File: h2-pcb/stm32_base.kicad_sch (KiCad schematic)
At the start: 42 parts, among them J1 Network Connector, J2 STDC14, SW1 SW_Push, U1 LD39050PU33R, U2 STM32G474RBT6, U3 SN65HVD230, Y1 8MHz

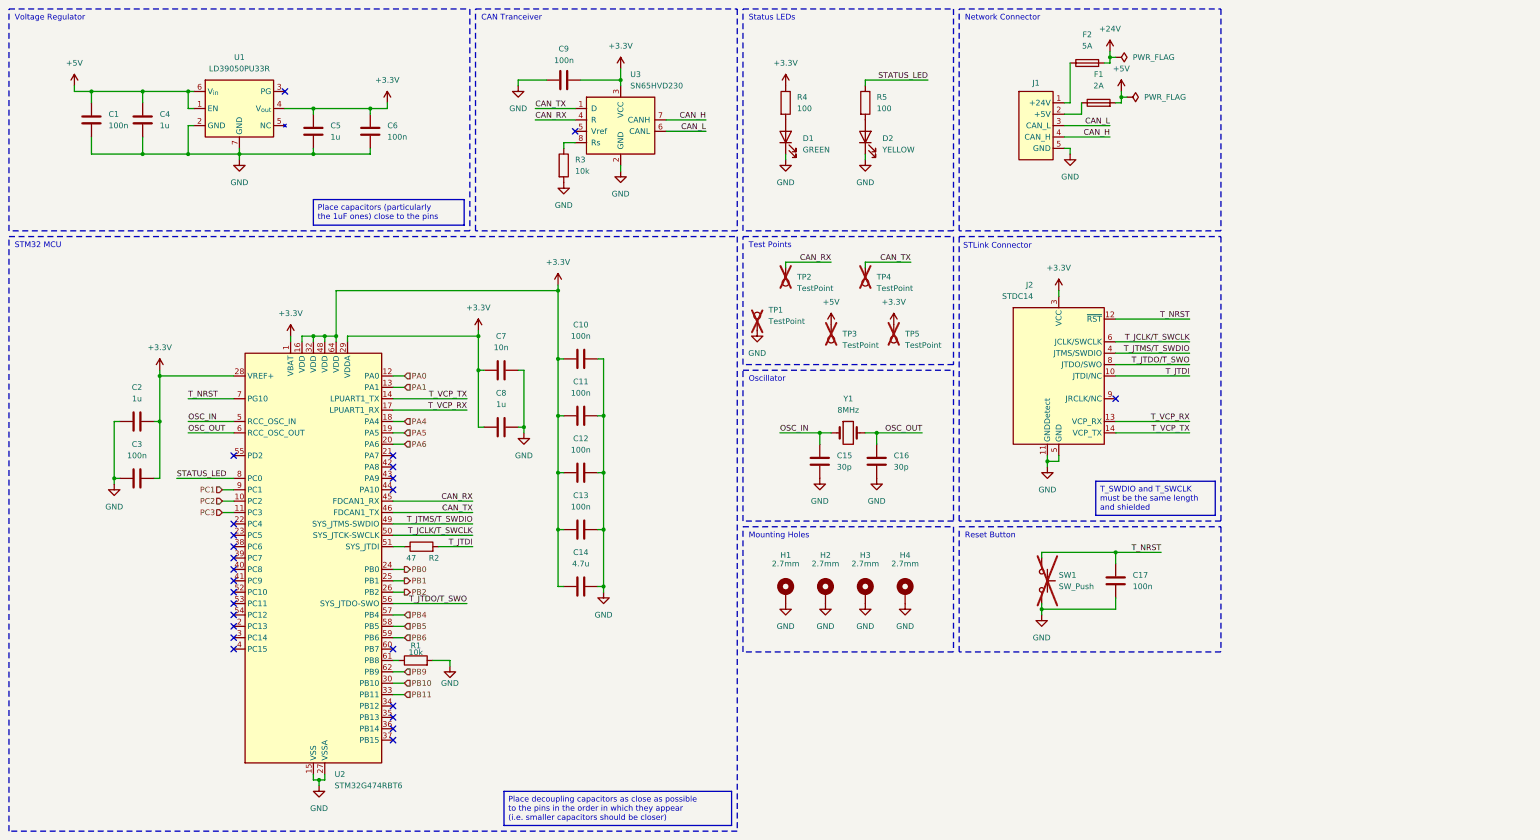
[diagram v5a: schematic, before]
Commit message: h2-pcb: add manometer, actuator and ds2428
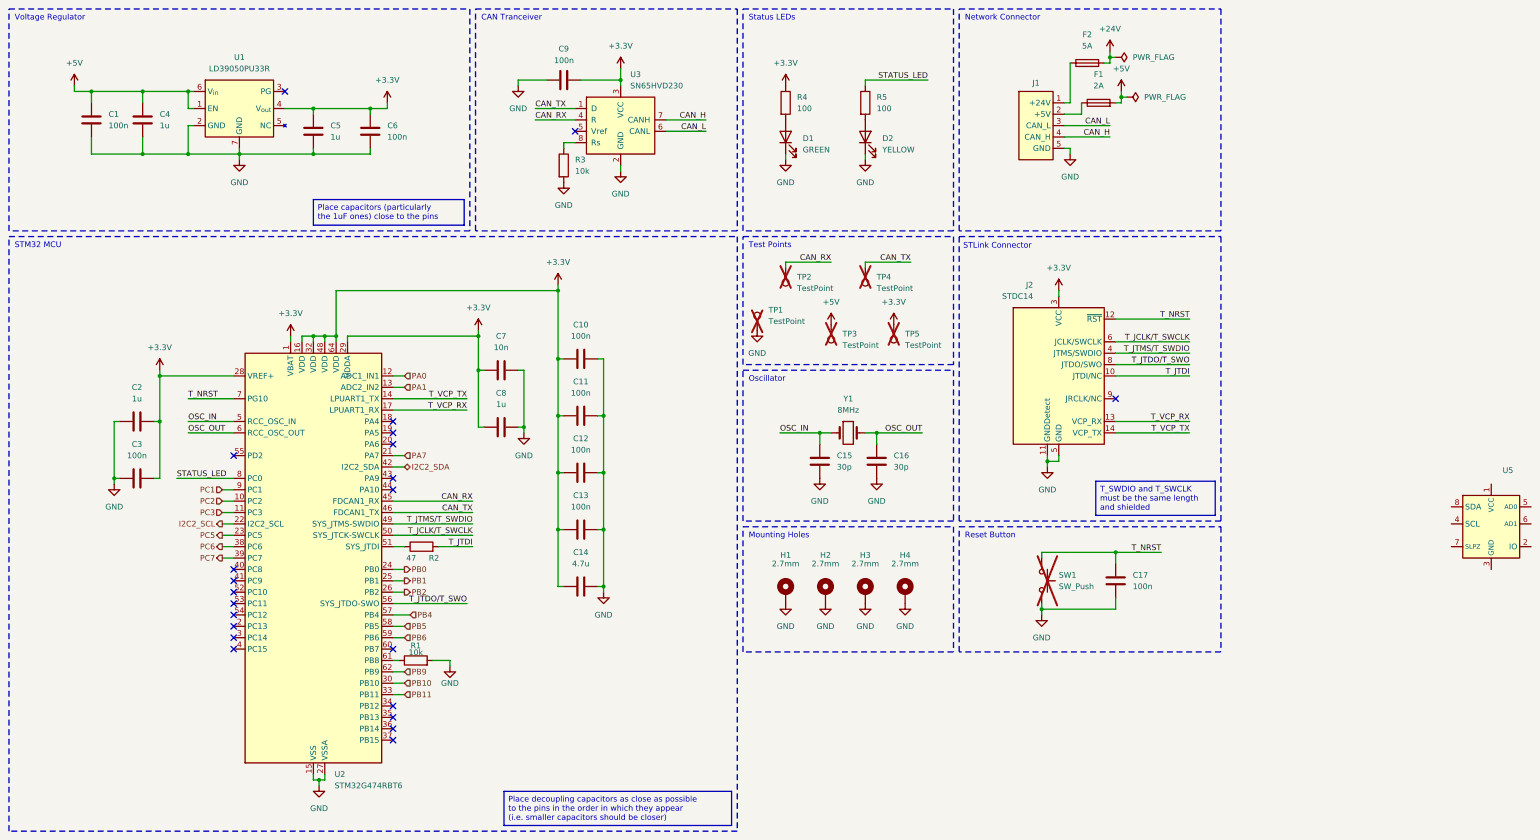
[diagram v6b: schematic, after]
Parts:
- added U5: ~, symbol DS2482-100:DS2482-100
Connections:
- net PA7: now reaches U2.21 (PA7)
- net I2C2_SCL: now reaches U2.22 (PC4)
- net PC5: now reaches U2.23 (PC5)
- net PC6: now reaches U2.38 (PC6)
- net PC7: now reaches U2.39 (PC7)
- net I2C2_SDA: now reaches U2.42 (PA8)
- net PA4: no longer names the net of U2.18 (PA4)
- net PA5: no longer names the net of U2.19 (PA5)
- net PA6: no longer names the net of U2.20 (PA6)
- no-connect marks 25 -> 22
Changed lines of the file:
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@@
 	)
 	(no_connect
-		(at 99.06 115.57)
-	)
-	(no_connect
 		(at 63.5 146.05)
 	)
 	(no_connect
-		(at 63.5 130.81)
-	)
-	(no_connect
 		(at 99.06 171.45)
 	)
@@
 	)
 	(no_connect
-		(at 63.5 128.27)
-	)
-	(no_connect
 		(at 99.06 120.65)
 	)
@@
 	)
 	(no_connect
+		(at 99.06 105.41)
+	)
+	(no_connect
 		(at 74.93 31.75)
 	)
@@
 	)
 	(no_connect
-		(at 63.5 133.35)
-	)
-	(no_connect
 		(at 99.06 176.53)
 	)
@@
 	)
 	(no_connect
-		(at 63.5 135.89)
-	)
-	(no_connect
-		(at 99.06 113.03)
+		(at 99.06 110.49)
 	)
 	(no_connect
@@
 	)
 	(no_connect
+		(at 99.06 107.95)
+	)
+	(no_connect
 		(at 63.5 151.13)
 	)
@@
 	(wire
 		(pts
-			(xy 99.06 105.41) (xy 101.6 105.41)
-		)
-		(stroke
-			(width 0)
-			(type default)
-		)
-	)
-	(wire
-		(pts
 			(xy 81.28 44.45) (xy 81.28 45.72)
 		)
@@
 	(wire
 		(pts
+			(xy 60.96 130.81) (xy 63.5 130.81)
+		)
+		(stroke
+			(width 0)
+			(type default)
+		)
+	)
+	(wire
+		(pts
 			(xy 144.78 142.24) (xy 146.05 142.24)
 		)
@@
 	(wire
 		(pts
+			(xy 60.96 128.27) (xy 63.5 128.27)
+		)
+		(stroke
+			(width 0)
+			(type default)
+		)
+	)
+	(wire
+		(pts
 			(xy 99.06 133.35) (xy 101.6 133.35)
 		)
@@
 	(wire
 		(pts
+			(xy 99.06 113.03) (xy 101.6 113.03)
+		)
+		(stroke
+			(width 0)
+			(type default)
+		)
+	)
+	(wire
+		(pts
 			(xy 82.55 185.42) (xy 81.28 185.42)
 		)
@@
 	(wire
 		(pts
-			(xy 99.06 148.59) (xy 101.6 148.59)
+			(xy 99.06 148.59) (xy 102.87 148.59)
 		)
 		(stroke
@@
 	(wire
 		(pts
+			(xy 60.96 135.89) (xy 63.5 135.89)
+		)
+		(stroke
+			(width 0)
+			(type default)
+		)
+	)
+	(wire
+		(pts
 			(xy 146.05 116.84) (xy 146.05 129.54)
 		)
@@
 	(wire
 		(pts
-			(xy 99.06 107.95) (xy 101.6 107.95)
-		)
-		(stroke
-			(width 0)
-			(type default)
-		)
-	)
-	(wire
-		(pts
 			(xy 118.11 86.36) (xy 118.11 93.98)
 		)
@@
 	(wire
 		(pts
+			(xy 60.96 133.35) (xy 63.5 133.35)
+		)
+		(stroke
+			(width 0)
+			(type default)
+		)
+	)
+	(wire
+		(pts
 			(xy 127 93.98) (xy 128.27 93.98)
 		)
@@
 	(wire
 		(pts
-			(xy 99.06 110.49) (xy 101.6 110.49)
+			(xy 135.89 142.24) (xy 137.16 142.24)
 		)
 		(stroke
@@
 	(wire
 		(pts
-			(xy 135.89 142.24) (xy 137.16 142.24)
+			(xy 99.06 123.19) (xy 116.84 123.19)
 		)
 		(stroke
@@
 	(wire
 		(pts
-			(xy 99.06 123.19) (xy 116.84 123.19)
+			(xy 186.69 71.12) (xy 186.69 69.85)
 		)
 		(stroke
@@
 	(wire
 		(pts
-			(xy 186.69 71.12) (xy 186.69 69.85)
+			(xy 99.06 115.57) (xy 101.6 115.57)
 		)
 		(stroke
@@
 		)
 	)
+	(hierarchical_label "I2C2_SDA"
+		(shape bidirectional)
+		(at 101.6 115.57 0)
+		(effects
+			(font
+				(size 1.27 1.27)
+			)
+			(justify left)
+		)
+	)
 	(hierarchical_label "PB2"
 		(shape output)
@@
 		)
 	)
-	(hierarchical_label "PA6"
+	(hierarchical_label "PC2"
 		(shape input)
-		(at 101.6 110.49 0)
+		(at 60.96 123.19 180)
 		(effects
 			(font
 				(size 1.27 1.27)
 			)
-			(justify left)
+			(justify right)
 		)
 	)
-	(hierarchical_label "PC2"
+	(hierarchical_label "PA7"
 		(shape input)
-		(at 60.96 123.19 180)
+		(at 101.6 113.03 0)
 		(effects
 			(font
 				(size 1.27 1.27)
 			)
-			(justify right)
+			(justify left)
 		)
 	)
-	(hierarchical_label "PB9"
-		(shape input)
-		(at 101.6 161.29 0)
+	(hierarchical_label "PC7"
+		(shape output)
+		(at 60.96 135.89 180)
 		(effects
 			(font
 				(size 1.27 1.27)
 			)
-			(justify left)
+			(justify right)
 		)
 	)
-	(hierarchical_label "PB10"
+	(hierarchical_label "PB9"
 		(shape input)
-		(at 101.6 163.83 0)
+		(at 101.6 161.29 0)
 		(effects
 			(font
@@
 		)
 	)
-	(hierarchical_label "PA4"
+	(hierarchical_label "PB10"
 		(shape input)
-		(at 101.6 105.41 0)
+		(at 101.6 163.83 0)
 		(effects
 			(font
@@
 	(hierarchical_label "PB4"
 		(shape input)
-		(at 101.6 148.59 0)
+		(at 102.87 148.59 0)
 		(effects
 			(font
@@
 		)
 	)
-	(hierarchical_label "PA5"
-		(shape input)
-		(at 101.6 107.95 0)
+	(hierarchical_label "PC6"
+		(shape output)
+		(at 60.96 133.35 180)
 		(effects
 			(font
 				(size 1.27 1.27)
 			)
-			(justify left)
+			(justify right)
+		)
+	)
+	(hierarchical_label "I2C2_SCL"
+		(shape output)
+		(at 60.96 128.27 180)
+		(effects
+			(font
+				(size 1.27 1.27)
+			)
+			(justify right)
+		)
+	)
+	(hierarchical_label "PC5"
+		(shape output)
+		(at 60.96 130.81 180)
+		(effects
+			(font
+				(size 1.27 1.27)
+			)
+			(justify right)
 		)
 	)
@@
 	)
 	(symbol
+		(lib_name "DS2482-100_1")
+		(lib_id "DS2482-100:DS2482-100")
+		(at 344.17 128.27 0)
+		(unit 1)
+		(exclude_from_sim no)
+		(in_bom yes)
+		(on_board yes)
+		(dnp no)
+		(property "Reference" "U5"
+			(at 346.71 116.332 0)
+			(effects
+				(font
+					(size 1.27 1.27)
+				)
+				(justify left)
+			)
+		)
+		(property "Value" "~"
+			(at 347.726 117.602 0)
+			(effects
+				(font
+					(size 1.27 1.27)
+				)
+				(justify left)
+			)
+		)
+		(property "Footprint" ""
+			(at 344.17 130.81 0)
+			(effects
+				(font
+					(size 1.27 1.27)
+				)
+				(hide yes)
+			)
+		)
+		(property "Datasheet" ""
+			(at 344.17 130.81 0)
+			(effects
+				(font
+					(size 1.27 1.27)
+				)
+				(hide yes)
+			)
+		)
+		(property "Description" ""
+			(at 344.17 130.81 0)
+			(effects
+				(font
+					(size 1.27 1.27)
+				)
+				(hide yes)
+			)
+		)
+		(pin "1"
+		)
+		(pin "2"
+		)
+		(pin "3"
+		)
+		(pin "4"
+		)
+		(pin "5"
+		)
+		(pin "6"
+		)
+		(pin "7"
+		)
+		(pin "8"
+		)
+		(instances
+			(project ""
+				(path "/4b4cf3aa-c94c-4150-b9c5-35049cd71136/7d59fd70-1fff-4c9c-ae77-583b08aef567"
+					(reference "U5")
+					(unit 1)
+				)
+			)
+		)
+	)
+	(symbol
 		(lib_id "power:PWR_FLAG")
 		(at 260.35 24.13 270)
@@
 		)
 		(pin "22"
+			(alternate "I2C2_SCL")
 		)
 		(pin "19"
@@
 		)
 		(pin "13"
+			(alternate "ADC2_IN2")
 		)
 		(pin "37"
@@
 		)
 		(pin "12"
+			(alternate "ADC1_IN1")
 		)
 		(pin "41"
 		)
 		(pin "42"
+			(alternate "I2C2_SDA")
 		)
 		(pin "5"

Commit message: Mosfets and Actuators dans truc pcb
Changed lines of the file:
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@@
 		)
 		(pin "35"
+			(alternate "ADC3_IN5")
 		)
 		(pin "1"

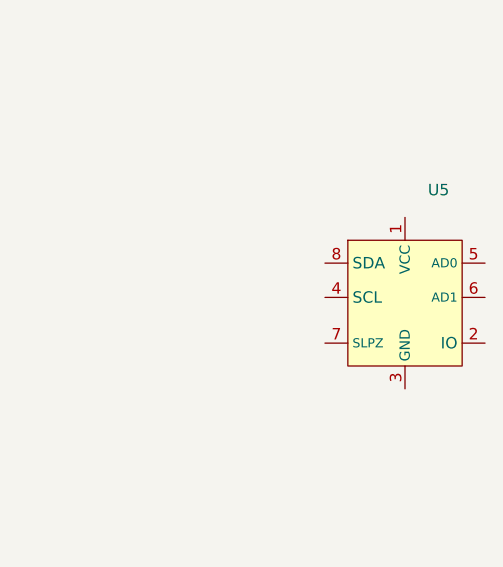
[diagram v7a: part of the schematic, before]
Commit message: Ajout des footprints aux composantes & update du pcb (routage almost done ?)
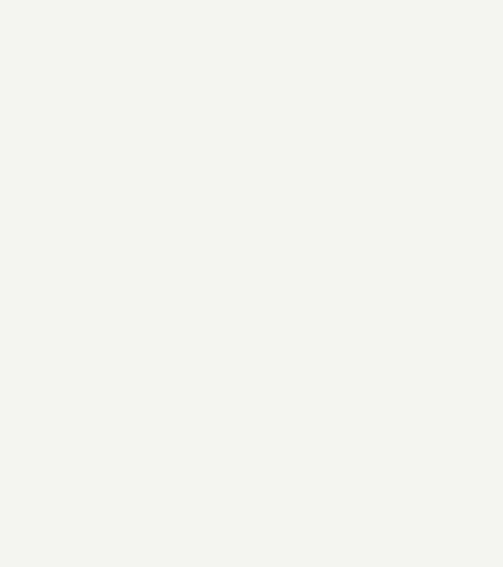
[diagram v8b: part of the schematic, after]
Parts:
- removed U5: ~, symbol DS2482-100:DS2482-100
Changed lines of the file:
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@@
-	)
-	(symbol
-		(lib_name "DS2482-100_1")
-		(lib_id "DS2482-100:DS2482-100")
-		(at 344.17 128.27 0)
-		(unit 1)
-		(exclude_from_sim no)
-		(in_bom yes)
-		(on_board yes)
-		(dnp no)
-		(property "Reference" "U5"
-			(at 346.71 116.332 0)
-			(effects
-				(font
-					(size 1.27 1.27)
-				)
-				(justify left)
-			)
-		)
-		(property "Value" "~"
-			(at 347.726 117.602 0)
-			(effects
-				(font
-					(size 1.27 1.27)
-				)
-				(justify left)
-			)
-		)
-		(property "Footprint" ""
-			(at 344.17 130.81 0)
-			(effects
-				(font
-					(size 1.27 1.27)
-				)
-				(hide yes)
-			)
-		)
-		(property "Datasheet" ""
-			(at 344.17 130.81 0)
-			(effects
-				(font
-					(size 1.27 1.27)
-				)
-				(hide yes)
-			)
-		)
-		(property "Description" ""
-			(at 344.17 130.81 0)
-			(effects
-				(font
-					(size 1.27 1.27)
-				)
-				(hide yes)
-			)
-		)
-		(pin "1"
-		)
-		(pin "2"
-		)
-		(pin "3"
-		)
-		(pin "4"
-		)
-		(pin "5"
-		)
-		(pin "6"
-		)
-		(pin "7"
-		)
-		(pin "8"
-		)
-		(instances
-			(project ""
-				(path "/4b4cf3aa-c94c-4150-b9c5-35049cd71136/7d59fd70-1fff-4c9c-ae77-583b08aef567"
-					(reference "U5")
-					(unit 1)
-				)
-			)
-		)
 	)
 	(symbol
